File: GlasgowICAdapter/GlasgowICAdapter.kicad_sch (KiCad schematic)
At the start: 2 parts, among them J1 PORT A, J2 PORT B

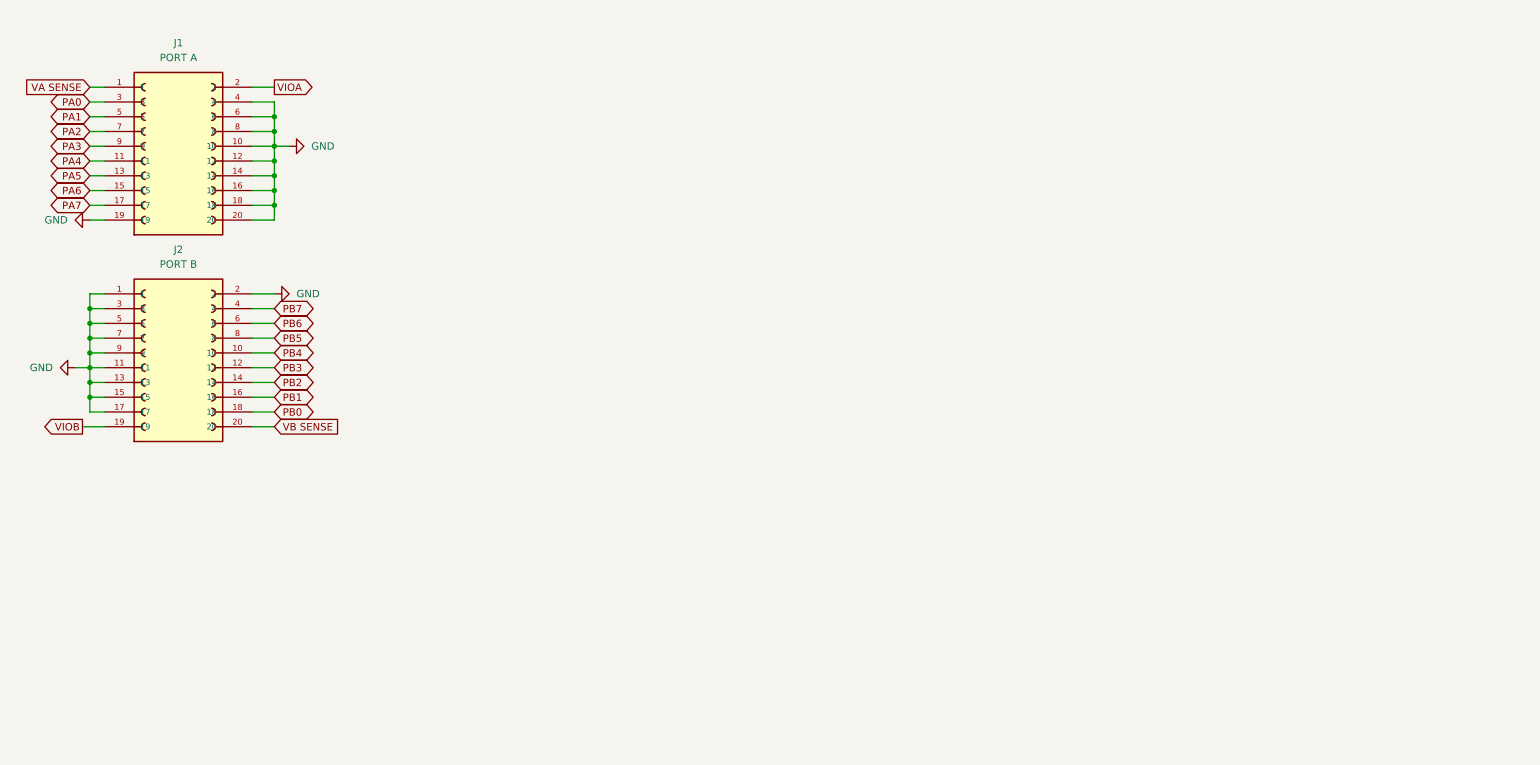
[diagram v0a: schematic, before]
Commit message: Added ZIF socket and chips, routed basics
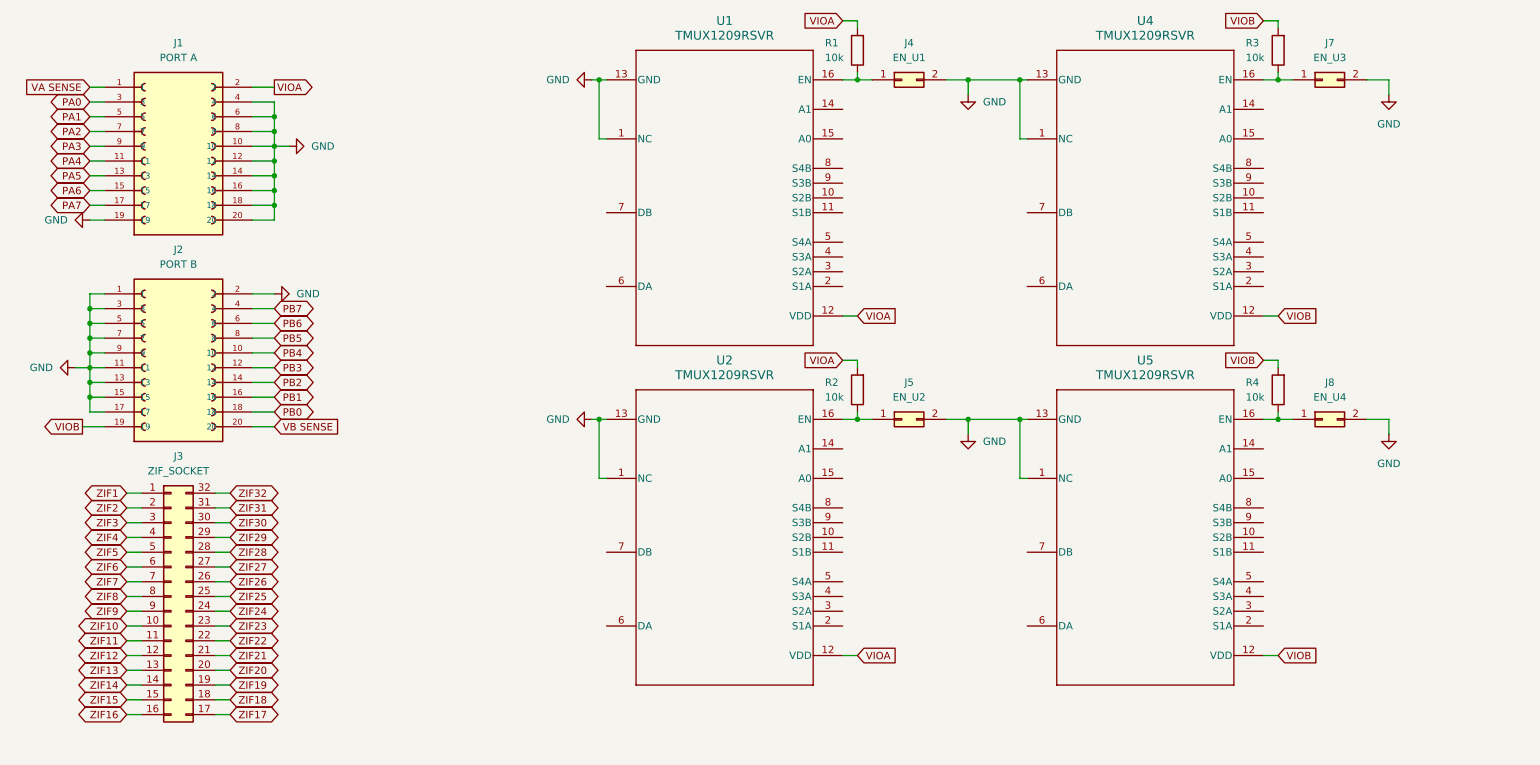
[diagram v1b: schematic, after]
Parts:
- added J3: ZIF_SOCKET, symbol Connector_Generic:Conn_02x16_Counter_Clockwise
- added J4: EN_U1, symbol Connector_Generic:Conn_02x01
- added J5: EN_U2, symbol Connector_Generic:Conn_02x01
- added J7: EN_U3, symbol Connector_Generic:Conn_02x01
- added J8: EN_U4, symbol Connector_Generic:Conn_02x01
- added R1, R2, R3, R4: 10k, symbol Device:R
- added U1, U2, U4, U5: TMUX1209RSVR, RSV0016A, symbol 2025-10-13_14-57-00:TMUX1209RSVR
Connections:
- net GND: now also J4.2 (Pin_2), J5.2 (Pin_2), J7.2 (Pin_2), J8.2 (Pin_2), U1.1 (NC), U1.13 (GND), U2.1 (NC), U2.13 (GND), U4.1 (NC), U4.13 (GND), U5.1 (NC), U5.13 (GND)
- net VIOA: now also R1.2, R2.2, U1.12 (VDD), U2.12 (VDD)
- net VIOB: now also R3.2, R4.2, U4.12 (VDD), U5.12 (VDD)
- new net: J4.1 (Pin_1), R1.1, U1.16 (EN)
- new net: J7.1 (Pin_1), R3.1, U4.16 (EN)
- new net: J5.1 (Pin_1), R2.1, U2.16 (EN)
- new net: J8.1 (Pin_1), R4.1, U5.16 (EN)
- new net ZIF1: J3.1 (Pin_1)
- new net ZIF10: J3.10 (Pin_10)
- new net ZIF11: J3.11 (Pin_11)
- new net ZIF12: J3.12 (Pin_12)
- new net ZIF13: J3.13 (Pin_13)
- new net ZIF14: J3.14 (Pin_14)
- new net ZIF15: J3.15 (Pin_15)
- new net ZIF16: J3.16 (Pin_16)
- new net ZIF17: J3.17 (Pin_17)
- new net ZIF18: J3.18 (Pin_18)
- new net ZIF19: J3.19 (Pin_19)
- new net ZIF2: J3.2 (Pin_2)
- new net ZIF20: J3.20 (Pin_20)
- new net ZIF21: J3.21 (Pin_21)
- new net ZIF22: J3.22 (Pin_22)
- new net ZIF23: J3.23 (Pin_23)
- new net ZIF24: J3.24 (Pin_24)
- new net ZIF25: J3.25 (Pin_25)
- new net ZIF26: J3.26 (Pin_26)
- new net ZIF27: J3.27 (Pin_27)
- new net ZIF28: J3.28 (Pin_28)
- new net ZIF29: J3.29 (Pin_29)
- new net ZIF3: J3.3 (Pin_3)
- new net ZIF30: J3.30 (Pin_30)
- new net ZIF31: J3.31 (Pin_31)
- new net ZIF32: J3.32 (Pin_32)
- new net ZIF4: J3.4 (Pin_4)
- new net ZIF5: J3.5 (Pin_5)
- new net ZIF6: J3.6 (Pin_6)
- new net ZIF7: J3.7 (Pin_7)
- new net ZIF8: J3.8 (Pin_8)
- new net ZIF9: J3.9 (Pin_9)

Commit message: Added IO ports for both ports and for ZIF socket
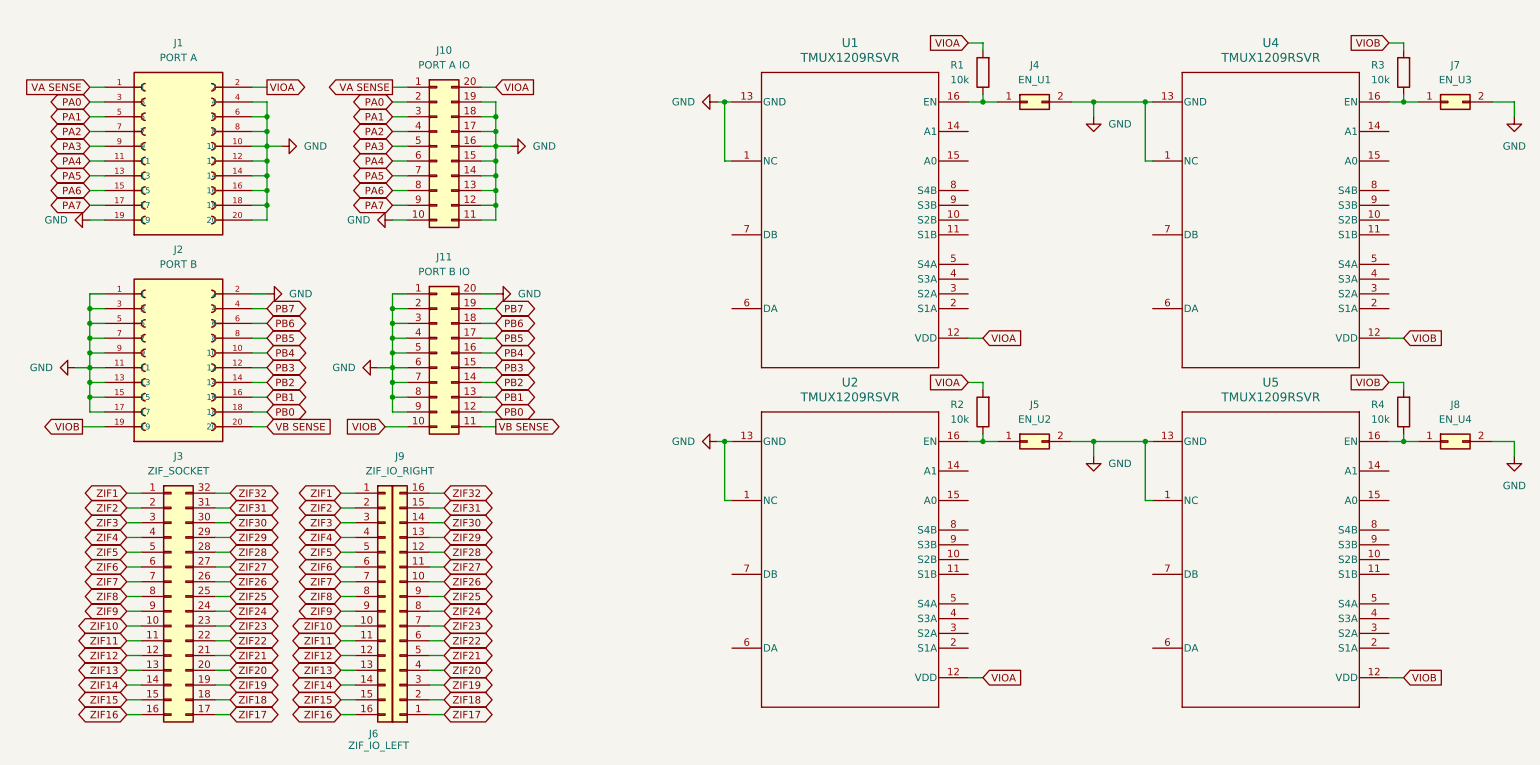
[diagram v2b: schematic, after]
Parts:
- added J10: PORT A IO, symbol Connector_Generic:Conn_02x10_Counter_Clockwise
- added J11: PORT B IO, symbol Connector_Generic:Conn_02x10_Counter_Clockwise
- added J6: ZIF_IO_LEFT, symbol Connector_Generic:Conn_01x16
- added J9: ZIF_IO_RIGHT, symbol Connector_Generic:Conn_01x16
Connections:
- net GND: now also J10.10 (Pin_10), J10.11 (Pin_11), J10.12 (Pin_12), J10.13 (Pin_13), J10.14 (Pin_14), J10.15 (Pin_15), J10.16 (Pin_16), J10.17 (Pin_17), J10.18 (Pin_18), J10.19 (Pin_19), J11.1 (Pin_1), J11.2 (Pin_2), J11.20 (Pin_20), J11.3 (Pin_3), J11.4 (Pin_4), J11.5 (Pin_5), J11.6 (Pin_6), J11.7 (Pin_7), J11.8 (Pin_8), J11.9 (Pin_9)
- net PA0: now also J10.2 (Pin_2)
- net PA1: now also J10.3 (Pin_3)
- net PA2: now also J10.4 (Pin_4)
- net PA3: now also J10.5 (Pin_5)
- net PA4: now also J10.6 (Pin_6)
- net PA5: now also J10.7 (Pin_7)
- net PA6: now also J10.8 (Pin_8)
- net PA7: now also J10.9 (Pin_9)
- net PB0: now also J11.12 (Pin_12)
- net PB1: now also J11.13 (Pin_13)
- net PB2: now also J11.14 (Pin_14)
- net PB3: now also J11.15 (Pin_15)
- net PB4: now also J11.16 (Pin_16)
- net PB5: now also J11.17 (Pin_17)
- net PB6: now also J11.18 (Pin_18)
- net PB7: now also J11.19 (Pin_19)
- net VA SENSE: now also J10.1 (Pin_1)
- net VB SENSE: now also J11.11 (Pin_11)
- net VIOA: now also J10.20 (Pin_20)
- net VIOB: now also J11.10 (Pin_10)
- net ZIF1: now also J6.1 (Pin_1)
- net ZIF10: now also J6.10 (Pin_10)
- net ZIF11: now also J6.11 (Pin_11)
- net ZIF12: now also J6.12 (Pin_12)
- net ZIF13: now also J6.13 (Pin_13)
- net ZIF14: now also J6.14 (Pin_14)
- net ZIF15: now also J6.15 (Pin_15)
- net ZIF16: now also J6.16 (Pin_16)
- net ZIF17: now also J9.1 (Pin_1)
- net ZIF18: now also J9.2 (Pin_2)
- net ZIF19: now also J9.3 (Pin_3)
- net ZIF2: now also J6.2 (Pin_2)
- net ZIF20: now also J9.4 (Pin_4)
- net ZIF21: now also J9.5 (Pin_5)
- net ZIF22: now also J9.6 (Pin_6)
- net ZIF23: now also J9.7 (Pin_7)
- net ZIF24: now also J9.8 (Pin_8)
- net ZIF25: now also J9.9 (Pin_9)
- net ZIF26: now also J9.10 (Pin_10)
- net ZIF27: now also J9.11 (Pin_11)
- net ZIF28: now also J9.12 (Pin_12)
- net ZIF29: now also J9.13 (Pin_13)
- net ZIF3: now also J6.3 (Pin_3)
- net ZIF30: now also J9.14 (Pin_14)
- net ZIF31: now also J9.15 (Pin_15)
- net ZIF32: now also J9.16 (Pin_16)
- net ZIF4: now also J6.4 (Pin_4)
- net ZIF5: now also J6.5 (Pin_5)
- net ZIF6: now also J6.6 (Pin_6)
- net ZIF7: now also J6.7 (Pin_7)
- net ZIF8: now also J6.8 (Pin_8)
- net ZIF9: now also J6.9 (Pin_9)
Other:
- moved on the sheet: J4, J5, J7, J8, R1, R2, R3, R4, U1, U2, U4, U5

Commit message: Finally connected everything together
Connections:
- net PA0: now also U1.15 (A0), U2.15 (A0)
- net PA1: now also U1.14 (A1), U2.14 (A1)
- net PA2: now also U1.7 (DB)
- net PA3: now also U1.6 (DA)
- net PA4: now also U2.7 (DB)
- net PA5: now also U2.6 (DA)
- net PB0: now also U4.15 (A0), U5.15 (A0)
- net PB1: now also U4.14 (A1), U5.14 (A1)
- net PB2: now also U4.7 (DB)
- net PB3: now also U4.6 (DA)
- net PB4: now also U5.7 (DB)
- net PB5: now also U5.6 (DA)
- net ZIF1: now also U1.8 (S4B)
- net ZIF10: now also U2.9 (S3B)
- net ZIF11: now also U2.10 (S2B)
- net ZIF12: now also U2.11 (S1B)
- net ZIF13: now also U2.5 (S4A)
- net ZIF14: now also U2.4 (S3A)
- net ZIF15: now also U2.3 (S2A)
- net ZIF16: now also U2.2 (S1A)
- net ZIF17: now also U4.8 (S4B)
- net ZIF18: now also U4.9 (S3B)
- net ZIF19: now also U4.10 (S2B)
- net ZIF2: now also U1.9 (S3B)
- net ZIF20: now also U4.11 (S1B)
- net ZIF21: now also U4.5 (S4A)
- net ZIF22: now also U4.4 (S3A)
- net ZIF23: now also U4.3 (S2A)
- net ZIF24: now also U4.2 (S1A)
- net ZIF25: now also U5.8 (S4B)
- net ZIF26: now also U5.9 (S3B)
- net ZIF27: now also U5.10 (S2B)
- net ZIF28: now also U5.11 (S1B)
- net ZIF29: now also U5.5 (S4A)
- net ZIF3: now also U1.10 (S2B)
- net ZIF30: now also U5.4 (S3A)
- net ZIF31: now also U5.3 (S2A)
- net ZIF32: now also U5.2 (S1A)
- net ZIF4: now also U1.11 (S1B)
- net ZIF5: now also U1.5 (S4A)
- net ZIF6: now also U1.4 (S3A)
- net ZIF7: now also U1.3 (S2A)
- net ZIF8: now also U1.2 (S1A)
- net ZIF9: now also U2.8 (S4B)
